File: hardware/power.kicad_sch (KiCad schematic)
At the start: 29 parts, among them J2 USB4085-GF-A, J3 B2B-PH-K-S, J4 PRPC001DAAN-RC, J5 PRPC001DAAN-RC, J6 PRPC001DAAN-RC, Q1 FDN338P, Q2 FDN338P, U1 USBLC6-2SC6, U2 TLV76733DGNR

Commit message: HW: Update components
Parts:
- C1: Voltage rating >200 V -> ≥200 V
- C2, C4: Digi-Key Part Number 490-7998-1-ND -> 732-7513-1-ND; Manufacturer Murata Electronics -> Würth Elektronik; Manufacturer Part Number GCM155R71C104KA55J -> 885012205018
- J2: value USB4085-GF-A -> USB4110-GF-A; footprint Connector_USB:USB_C_Receptacle_GCT_USB4085 -> Connector_USB:USB_C_Receptacle_GCT_USB4110; Digi-Key Part Number 2073-USB4085-GF-ACT-ND -> 2073-USB4110-GF-A-1-ND; Manufacturer Part Number USB4085-GF-A -> USB4110-GF-A
- LED1: value LS T67K-K1L2-1-0-2-R18-Z -> 150141YS73100; Digi-Key Part Number 475-LST67K-K1L2-1-ZCT-ND -> 732-5004-1-ND; Manufacturer ams-OSRAM USA INC. -> Würth Elektronik; Manufacturer Part Number LS T67K-K1L2-1-0-2-R18-Z -> 150141YS73100
- Q1, Q2: value FDN338P -> IRLML2246TRPBF; Digi-Key Part Number FDN338PCT-ND -> IRLML2246TRPBFCT-ND; Manufacturer onsemi -> Infineon Technologies; Manufacturer Part Number FDN338P -> IRLML2246TRPBF
- R1: Digi-Key Part Number RHM1.0MPCT-ND -> 732-560112132011CT-ND; Manufacturer Rohm Semiconductor -> Würth Elektronik; Manufacturer Part Number KTR18EZPJ105 -> 560112132011; Power rating 0.25 W -> ≥0.25 W; Working voltage 200 V -> ≥200 V
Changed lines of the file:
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@@
 	)
 	(junction
-		(at 157.48 64.77)
+		(at 78.74 119.38)
 		(diameter 0)
 		(color 0 0 0 0)
 	)
 	(junction
-		(at 184.15 73.66)
+		(at 157.48 64.77)
 		(diameter 0)
 		(color 0 0 0 0)
 	)
 	(junction
-		(at 125.73 64.77)
+		(at 184.15 73.66)
 		(diameter 0)
 		(color 0 0 0 0)
 	)
 	(junction
-		(at 212.09 52.07)
+		(at 125.73 64.77)
 		(diameter 0)
 		(color 0 0 0 0)
 	)
 	(junction
-		(at 72.39 119.38)
+		(at 212.09 52.07)
 		(diameter 0)
 		(color 0 0 0 0)
@@
 	(wire
 		(pts
-			(xy 72.39 119.38) (xy 96.52 119.38)
+			(xy 107.95 73.66) (xy 114.3 73.66)
 		)
 		(stroke
@@
 	(wire
 		(pts
-			(xy 107.95 73.66) (xy 114.3 73.66)
+			(xy 157.48 57.15) (xy 157.48 64.77)
 		)
 		(stroke
@@
 	(wire
 		(pts
-			(xy 157.48 57.15) (xy 157.48 64.77)
+			(xy 107.95 119.38) (xy 128.27 119.38)
 		)
 		(stroke
@@
 	(wire
 		(pts
-			(xy 107.95 119.38) (xy 128.27 119.38)
+			(xy 109.22 49.53) (xy 109.22 57.15)
 		)
 		(stroke
@@
 	(wire
 		(pts
-			(xy 109.22 49.53) (xy 109.22 57.15)
+			(xy 189.23 49.53) (xy 194.31 49.53)
 		)
 		(stroke
@@
 	(wire
 		(pts
-			(xy 189.23 49.53) (xy 194.31 49.53)
+			(xy 203.2 57.15) (xy 203.2 119.38)
 		)
 		(stroke
@@
 	(wire
 		(pts
-			(xy 203.2 57.15) (xy 203.2 119.38)
+			(xy 99.06 116.84) (xy 99.06 119.38)
 		)
 		(stroke
@@
 	(wire
 		(pts
-			(xy 99.06 116.84) (xy 99.06 119.38)
+			(xy 78.74 111.76) (xy 72.39 111.76)
 		)
 		(stroke
@@
 	(wire
 		(pts
-			(xy 72.39 111.76) (xy 72.39 119.38)
+			(xy 78.74 111.76) (xy 78.74 119.38)
 		)
 		(stroke
@@
 	(wire
 		(pts
+			(xy 78.74 119.38) (xy 96.52 119.38)
+		)
+		(stroke
+			(width 0)
+			(type default)
+		)
+	)
+	(wire
+		(pts
 			(xy 194.31 52.07) (xy 194.31 69.85)
 		)
@@
 	(wire
 		(pts
-			(xy 68.58 119.38) (xy 72.39 119.38)
+			(xy 68.58 119.38) (xy 78.74 119.38)
 		)
 		(stroke
@@
 		(dnp no)
 		(property "Reference" "C1"
-			(at 70.866 111.76 0)
+			(at 70.866 112.776 0)
 			(effects
 				(font
@@
 		)
 		(property "Value" "4.7 nF"
-			(at 70.866 113.538 0)
+			(at 70.866 114.808 0)
 			(effects
 				(font
@@
 			)
 		)
-		(property "Voltage rating" ">200 V"
-			(at 74.676 117.602 0)
+		(property "Voltage rating" "≥200 V"
+			(at 74.676 118.364 0)
 			(effects
 				(font
@@
 		)
 		(property "Tolerance" "±10 %"
-			(at 74.168 115.57 0)
+			(at 74.168 116.586 0)
 			(effects
 				(font
@@
 			)
 		)
-		(property "Manufacturer" "Murata Electronics"
+		(property "Manufacturer" "Würth Elektronik"
 			(at 153.67 77.47 0)
 			(effects
@@
 			)
 		)
-		(property "Manufacturer Part Number" "GCM155R71C104KA55J"
+		(property "Manufacturer Part Number" "885012205018"
 			(at 153.67 77.47 0)
 			(effects
@@
 			)
 		)
-		(property "Digi-Key Part Number" "490-7998-1-ND"
+		(property "Digi-Key Part Number" "732-7513-1-ND"
 			(at 153.67 77.47 0)
 			(effects
@@
 			)
 		)
-		(property "Manufacturer" "Rohm Semiconductor"
+		(property "Manufacturer" "Würth Elektronik"
 			(at 64.77 115.57 0)
 			(effects
@@
 			)
 		)
-		(property "Manufacturer Part Number" "KTR18EZPJ105"
+		(property "Manufacturer Part Number" "560112132011"
 			(at 64.77 115.57 0)
 			(effects
@@
 			)
 		)
-		(property "Digi-Key Part Number" "RHM1.0MPCT-ND"
+		(property "Digi-Key Part Number" "732-560112132011CT-ND"
 			(at 64.77 115.57 0)
 			(effects
@@
 			)
 		)
-		(property "Power rating" "0.25 W"
-			(at 59.944 115.57 0)
+		(property "Power rating" "≥0.25 W"
+			(at 59.182 115.57 0)
 			(effects
 				(font
@@
 			)
 		)
-		(property "Working voltage" "200 V"
-			(at 59.944 117.602 0)
+		(property "Working voltage" "≥200 V"
+			(at 59.436 117.602 0)
 			(effects
 				(font
@@
 			)
 		)
-		(property "Manufacturer" "Murata Electronics"
+		(property "Manufacturer" "Würth Elektronik"
 			(at 128.27 77.47 0)
 			(effects
@@
 			)
 		)
-		(property "Manufacturer Part Number" "GCM155R71C104KA55J"
+		(property "Manufacturer Part Number" "885012205018"
 			(at 128.27 77.47 0)
 			(effects
@@
 			)
 		)
-		(property "Digi-Key Part Number" "490-7998-1-ND"
+		(property "Digi-Key Part Number" "732-7513-1-ND"
 			(at 128.27 77.47 0)
 			(effects
@@
 			)
 		)
-		(property "Value" "USB4085-GF-A"
+		(property "Value" "USB4110-GF-A"
 			(at 54.102 90.424 0)
 			(effects
@@
 			)
 		)
-		(property "Footprint" "Connector_USB:USB_C_Receptacle_GCT_USB4085"
+		(property "Footprint" "Connector_USB:USB_C_Receptacle_GCT_USB4110"
 			(at 76.2 88.9 0)
 			(effects
@@
 			)
 		)
-		(property "Digi-Key Part Number" "2073-USB4085-GF-ACT-ND"
+		(property "Digi-Key Part Number" "2073-USB4110-GF-A-1-ND"
 			(at 72.39 88.9 0)
 			(effects
@@
 			)
 		)
-		(property "Manufacturer Part Number" "USB4085-GF-A"
+		(property "Manufacturer Part Number" "USB4110-GF-A"
 			(at 72.39 88.9 0)
 			(effects
@@
 			)
 		)
-		(property "Value" "FDN338P"
+		(property "Value" "IRLML2246TRPBF"
 			(at 157.48 46.482 90)
 			(effects
@@
 			)
 		)
-		(property "Digi-Key Part Number" "FDN338PCT-ND"
+		(property "Digi-Key Part Number" "IRLML2246TRPBFCT-ND"
 			(at 157.48 52.07 0)
 			(effects
@@
 			)
 		)
-		(property "Manufacturer" "onsemi"
+		(property "Manufacturer" "Infineon Technologies"
 			(at 157.48 52.07 0)
 			(effects
@@
 			)
 		)
-		(property "Manufacturer Part Number" "FDN338P"
+		(property "Manufacturer Part Number" "IRLML2246TRPBF"
 			(at 157.48 52.07 0)
 			(effects
@@
 			)
 		)
-		(property "Value" "FDN338P"
+		(property "Value" "IRLML2246TRPBF"
 			(at 125.73 46.482 90)
 			(effects
@@
 			)
 		)
-		(property "Digi-Key Part Number" "FDN338PCT-ND"
+		(property "Digi-Key Part Number" "IRLML2246TRPBFCT-ND"
 			(at 125.73 52.07 0)
 			(effects
@@
 			)
 		)
-		(property "Manufacturer" "onsemi"
+		(property "Manufacturer" "Infineon Technologies"
 			(at 125.73 52.07 0)
 			(effects
@@
 			)
 		)
-		(property "Manufacturer Part Number" "FDN338P"
+		(property "Manufacturer Part Number" "IRLML2246TRPBF"
 			(at 125.73 52.07 0)
 			(effects
@@
 			)
 		)
-		(property "Value" "LS T67K-K1L2-1-0-2-R18-Z"
+		(property "Value" "150141YS73100"
 			(at 226.695 60.96 90)
 			(effects
@@
 			)
 		)
-		(property "Manufacturer" "ams-OSRAM USA INC."
+		(property "Manufacturer" "Würth Elektronik"
 			(at 232.41 59.69 90)
 			(effects
@@
 			)
 		)
-		(property "Manufacturer Part Number" "LS T67K-K1L2-1-0-2-R18-Z"
+		(property "Manufacturer Part Number" "150141YS73100"
 			(at 232.41 59.69 90)
 			(effects
@@
 			)
 		)
-		(property "Digi-Key Part Number" "475-LST67K-K1L2-1-ZCT-ND"
+		(property "Digi-Key Part Number" "732-5004-1-ND"
 			(at 232.41 59.69 90)
 			(effects

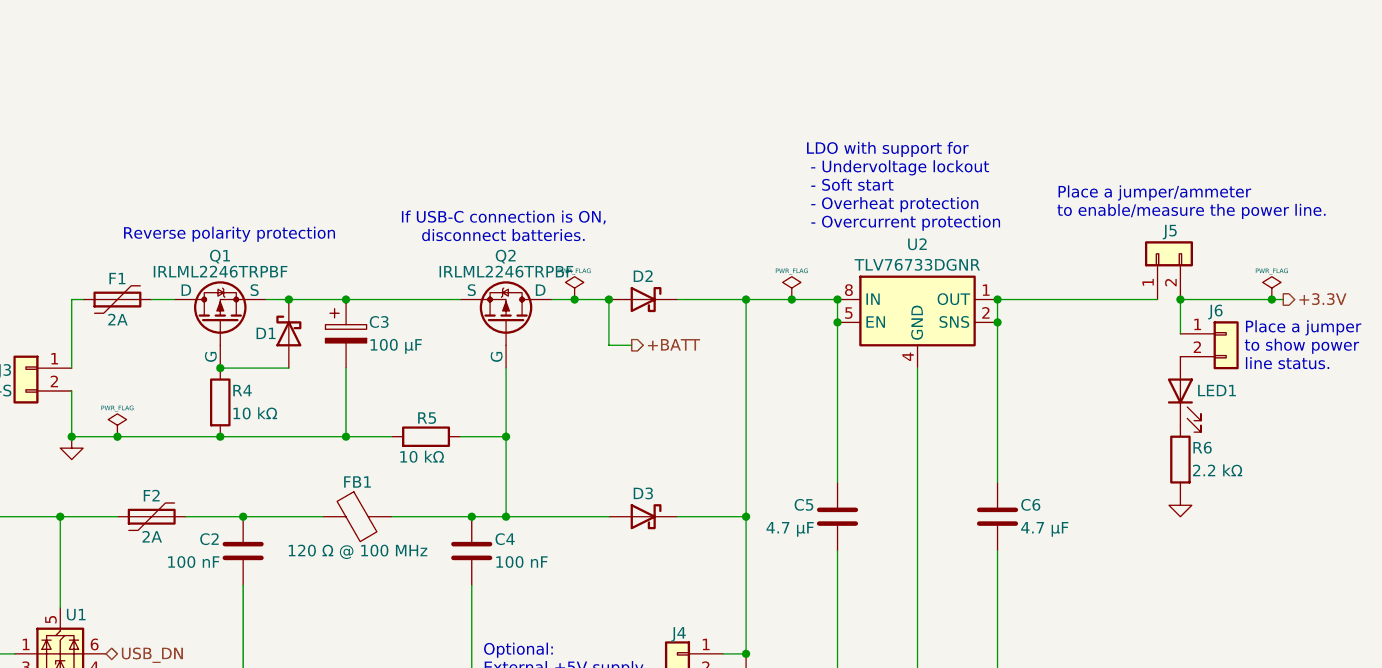
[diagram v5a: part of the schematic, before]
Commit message: HW: Update VBAT, schema and layout
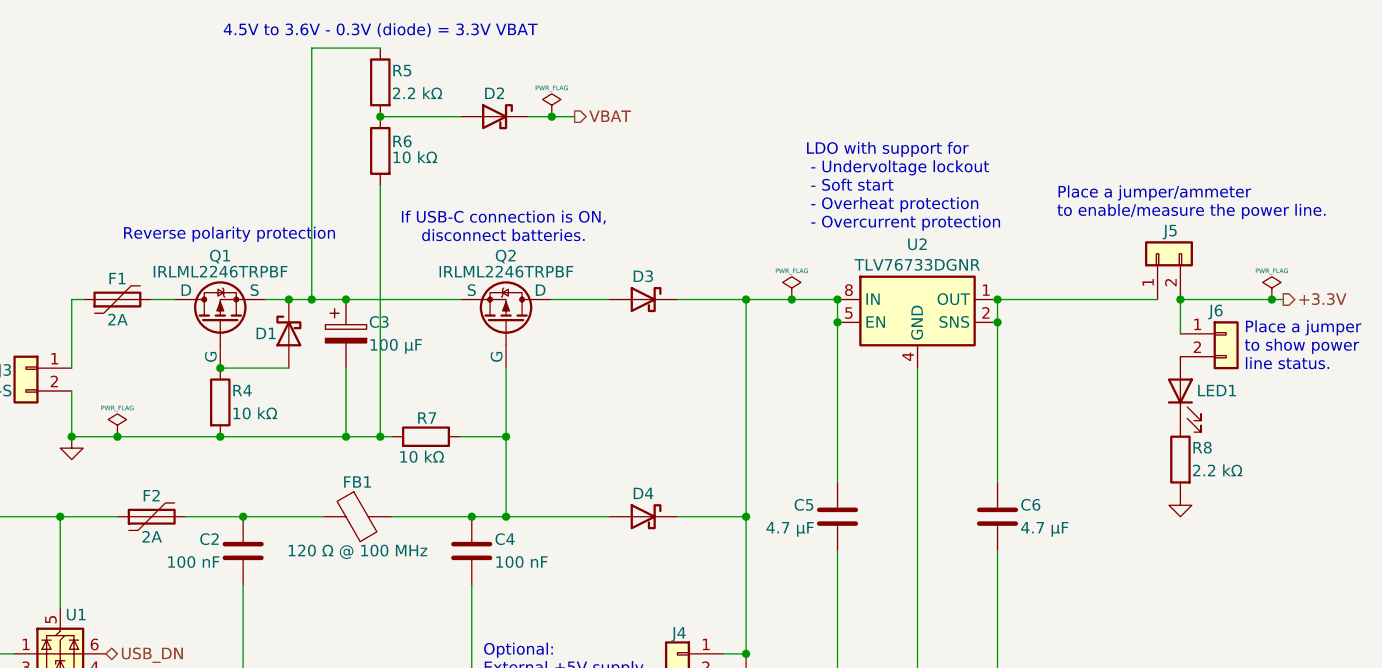
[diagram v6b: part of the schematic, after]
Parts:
- added D2: CDBA140LL-HF, Diode_SMD:D_SMA, symbol Device:D_Schottky
- added R5: 2.2 kΩ, perfect_footprints:0402_1005_perfect, symbol Device:R
- added R6: 10 kΩ, perfect_footprints:0402_1005_perfect, symbol Device:R
- renumbered D2 to D3, D3 to D4, R5 to R7, R6 to R8
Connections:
- net GND: now also R6.2
- net at C3.1, D1.1 (K), Q1.3 (S)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: now also R5.1
- net +BATT: no longer names the net of D3.2 (A), Q2.1 (D)
- new net: D2.2 (A), R5.2, R6.1
- new net VBAT: D2.1 (K)
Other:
- note added: "4.5V to 3.6V - 0.3V (diode) = 3.3V VBAT"

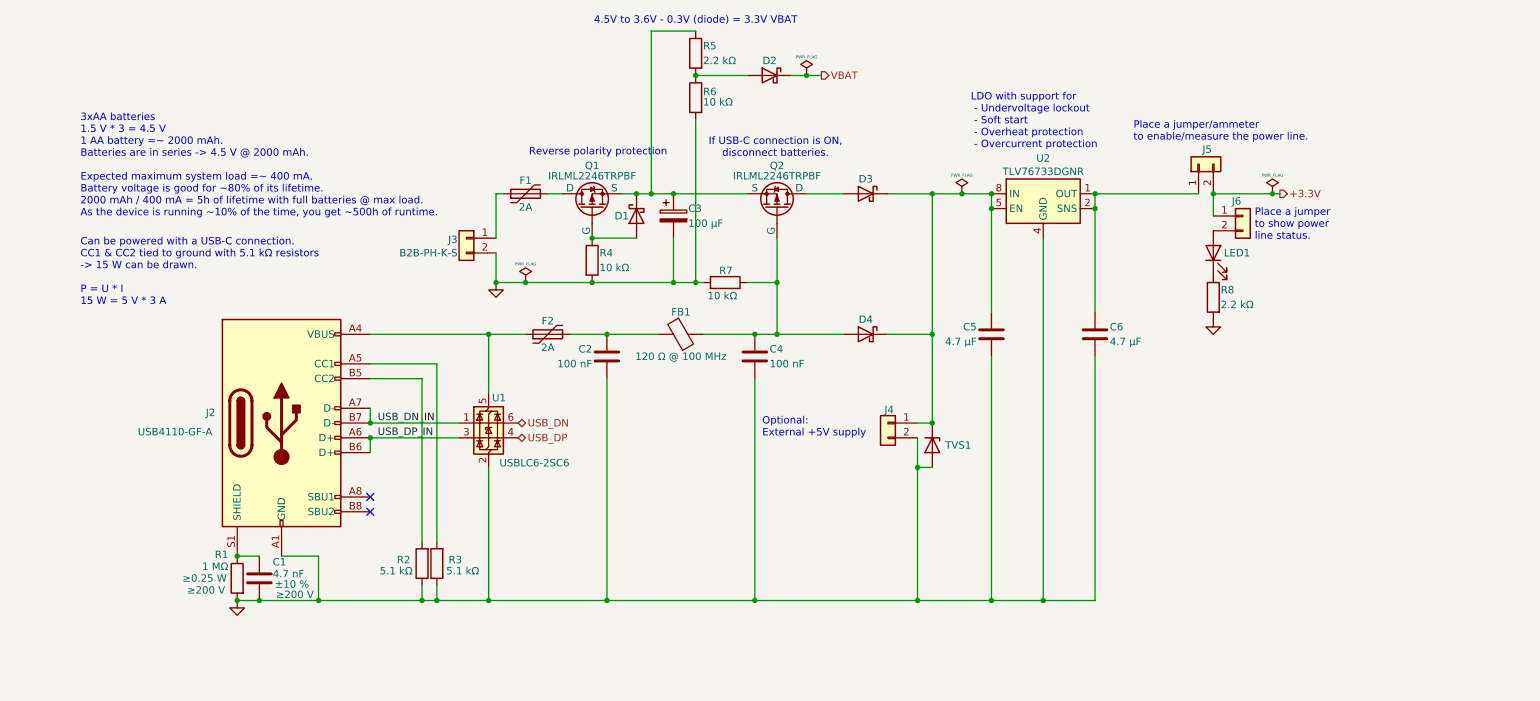
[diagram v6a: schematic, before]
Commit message: HW: Start adding Li-Po support
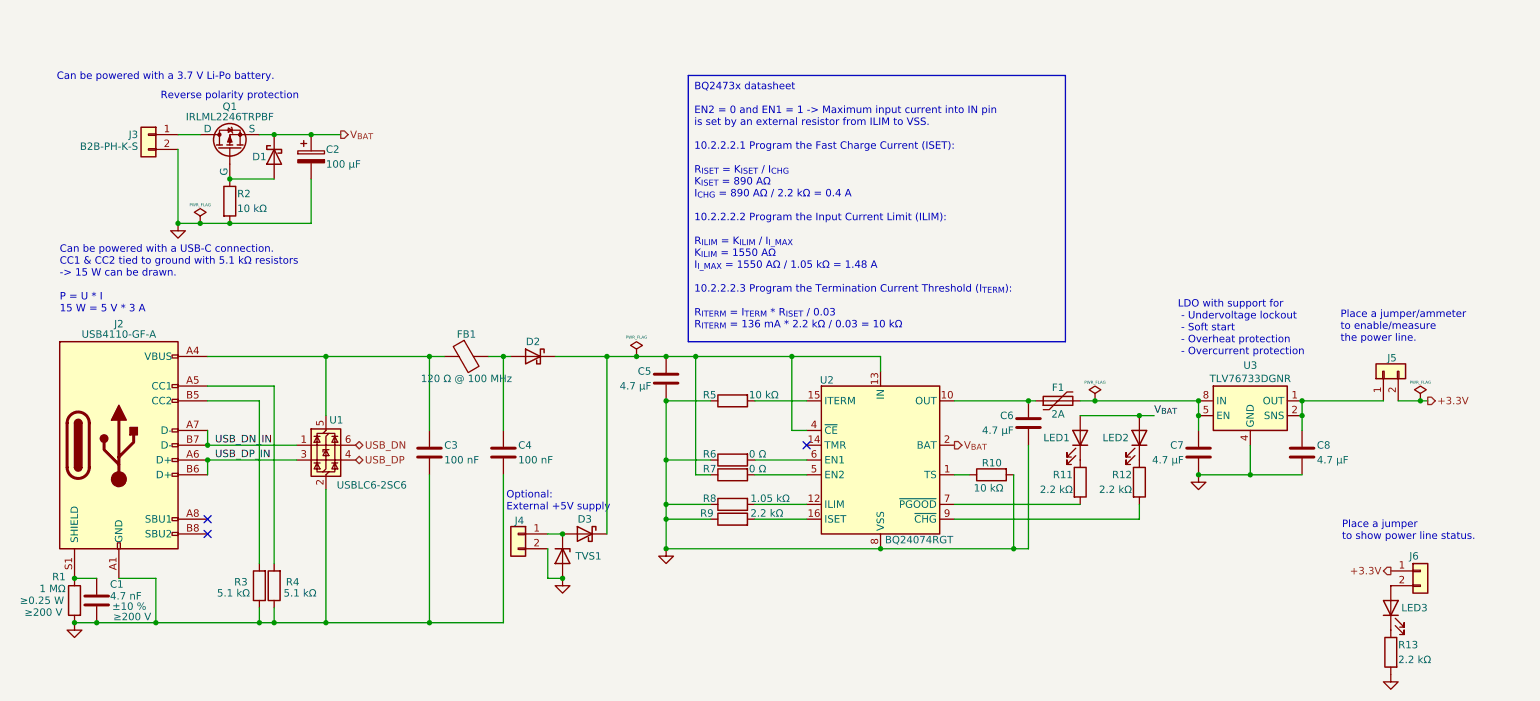
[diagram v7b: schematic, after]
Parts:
- removed D2: CDBA140LL-HF, Diode_SMD:D_SMA, symbol Device:D_Schottky
- removed F2: 2A, Fuse:Fuse_0805_2012Metric, symbol Device:Polyfuse
- removed Q2: IRLML2246TRPBF, Package_TO_SOT_SMD:SOT-23-3, symbol Simulation_SPICE:PMOS
- added C5, C6: 4.7 µF, Capacitor_SMD:C_0603_1608Metric, symbol Device:C
- added LED1, LED2: 150141YS73100, LED_SMD:LED_PLCC_2835, symbol Device:LED
- added R10: 10 kΩ, perfect_footprints:0402_1005_perfect, symbol Device:R
- added R11, R12, R9: 2.2 kΩ, perfect_footprints:0402_1005_perfect, symbol Device:R
- added R8: 1.05 kΩ, perfect_footprints:0402_1005_perfect, symbol Device:R
- added U2: BQ24074RGT, Package_DFN_QFN:VQFN-16-1EP_3x3mm_P0.5mm_EP1.68x1.68mm, symbol Battery_Management:BQ24074RGT
- R5: value 2.2 kΩ -> 10 kΩ; Digi-Key Part Number 311-2.20KLRCT-ND -> 311-10.0KLRCT-ND; Manufacturer Part Number RC0402FR-072K2L -> RC0402FR-0710KL
- R6, R7: value 10 kΩ -> 0 Ω; Digi-Key Part Number 311-10.0KLRCT-ND -> 311-0.0JRCT-ND; Manufacturer Part Number RC0402FR-0710KL -> RC0402JR-070RL
- renumbered C3 to C2, C2 to C3, C5 to C7, C6 to C8, D4 to D2, LED1 to LED3, R8 to R13, R4 to R2, R2 to R3, R3 to R4, U2 to U3
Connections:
- net GND: now also R5.1, R6.1, C5.2, C6.2, R10.2, R8.1, R9.1, U2.17 (VSS), U2.8 (VSS); no longer R6.2, R7.2
- net at J2.A4 (VBUS), J2.A9 (VBUS), J2.B4 (VBUS)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: now also C3.1, FB1.1
- net V_{BAT}: now reaches C2.1, D1.1 (K), Q1.3 (S)
- net V_{BAT}: now also LED1.2 (A), LED2.2 (A), U2.2 (BAT), U2.3 (BAT); no longer R5.1
- net at R5.2: now also U2.15 (ITERM); no longer R6.1
- net at F1.1: now also C6.1, U2.10 (OUT), U2.11 (OUT); no longer J3.1 (Pin_1)
- net at F1.2: now also C7.1, U3.5 (EN), U3.8 (IN); no longer Q1.1 (D)
- net at C4.1, D2.2 (A), FB1.2: no longer R7.1
- net at D3.2 (A): now also J4.1 (Pin_1), TVS1.1 (K)
- new net: LED2.1 (K), R12.1
- new net: R8.2, U2.12 (ILIM)
- new net: R6.2, U2.6 (EN1)
- new net: J3.1 (Pin_1), Q1.1 (D)
- new net: C5.1, D2.1 (K), D3.1 (K), R7.1, U2.13 (IN), U2.4 (~{CE})
- new net: R7.2, U2.5 (EN2)
- new net: R9.2, U2.16 (ISET)
- new net: R10.1, U2.1 (TS)
- new net: LED1.1 (K), R11.1
- new net: R11.2, U2.7 (~{PGOOD})
- new net: R12.2, U2.9 (~{CHG})
- no-connect marks 2 -> 3
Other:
- note added: "Can be powered with a 3.7 V Li-Po battery."
- note removed: "3xAA batteries 1.5 V * 3 = 4.5 V 1 AA battery =~ 2000 mAh. Batteries are in series -> 4.5 V @ 2000 mAh. Expected maximum system load =~ 400 mA. Battery voltage is good for ~80% of its lifetime. 2000 mAh / 400 mA = 5h of lifetime with full batteries @ max load. As the device is running ~10% of the time, you get ~500h of runtime."
- note removed: "4.5V to 3.6V - 0.3V (diode) = 3.3V VBAT"
- note removed: "If USB-C connection is ON, disconnect batteries."
- moved on the sheet: C1, C2, C3, C4, C7, C8, D1, D2, F1, FB1, J2, J4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

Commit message: HW: Fix 5.1K USB resistors
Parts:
- R3, R4: Digi-Key Part Number 311-5.10KHRCT-ND -> 311-5.10KLRCT-ND; Manufacturer Part Number RC0603FR-075K1L -> RC0402FR-075K1L
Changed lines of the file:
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@@
 			)
 		)
-		(property "Manufacturer Part Number" "RC0603FR-075K1L"
+		(property "Manufacturer Part Number" "RC0402FR-075K1L"
 			(at 71.12 116.84 0)
 			(effects
@@
 			)
 		)
-		(property "Digi-Key Part Number" "311-5.10KHRCT-ND"
+		(property "Digi-Key Part Number" "311-5.10KLRCT-ND"
 			(at 71.12 116.84 0)
 			(effects
@@
 			)
 		)
-		(property "Manufacturer Part Number" "RC0603FR-075K1L"
+		(property "Manufacturer Part Number" "RC0402FR-075K1L"
 			(at 68.58 116.84 0)
 			(effects
@@
 			)
 		)
-		(property "Digi-Key Part Number" "311-5.10KHRCT-ND"
+		(property "Digi-Key Part Number" "311-5.10KLRCT-ND"
 			(at 68.58 116.84 0)
 			(effects
